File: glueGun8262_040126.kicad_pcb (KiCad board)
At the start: 2 copper layers, 104 x 93 mm, 73 parts, among them CN1 KF243-5.0-2P, CN2 KF243-5.0-2P, CN3 KF243-5.0-2P, CN4 KF243-5.0-2P, CN5 KF243-5.0-2P, CN6 KF243-5.0-2P, CN7 KF243-5.0-2P, CN9 KF243-5.0-4P, Q1 SQM120P10-10m1L, U1 DRV8262DDWR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

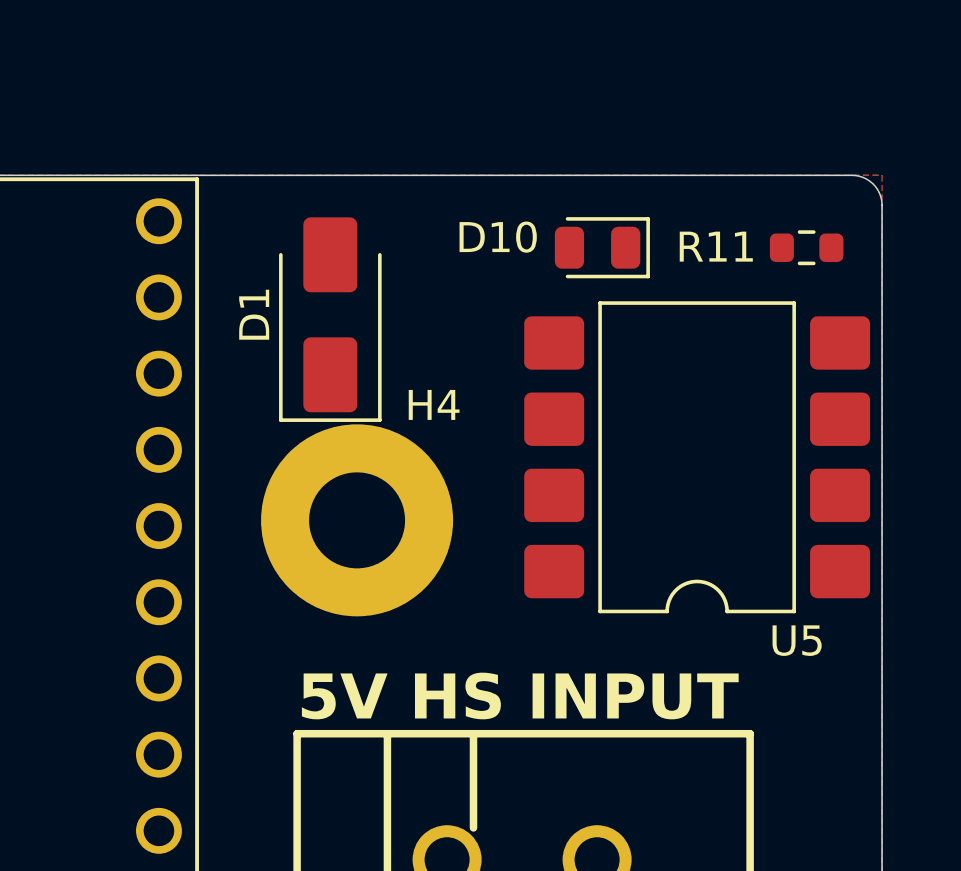
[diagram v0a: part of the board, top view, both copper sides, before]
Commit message: minor relocation
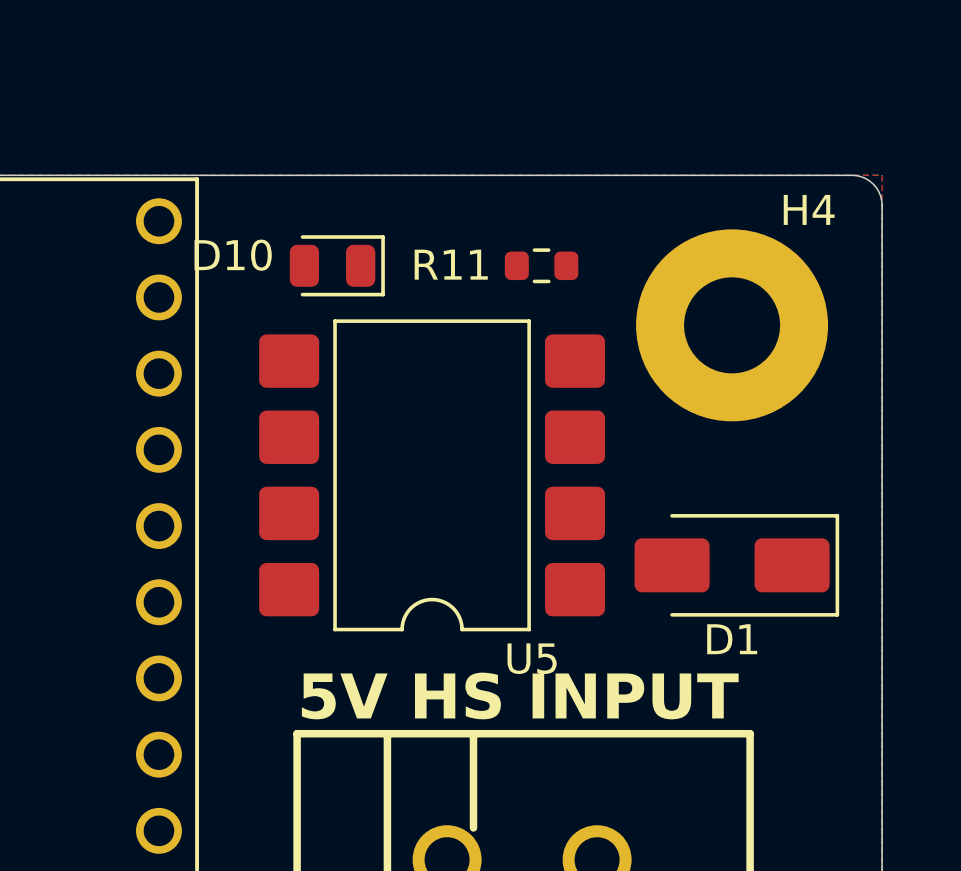
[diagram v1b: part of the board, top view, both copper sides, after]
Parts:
- moved D1 15.8 mm to (205.0, 53.0), turned to 180 degrees
- moved H4 14.1 mm to (205.0, 45.0)
- moved D10 8.86 mm to (191.7, 43.0)
- moved R11 8.86 mm to (198.7, 43.0)
- moved U5 8.86 mm to (195.0, 50.0)
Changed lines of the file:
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@@
 	(footprint "Resistor_SMD:R_0603_1608Metric"
 		(layer "F.Cu")
-		(at 207.4863 42.4125)
+		(at 198.6513 43.015)
 		(descr "Resistor SMD 0603 (1608 Metric), square (rectangular) end terminal, IPC-7351 nominal, (Body size source: IPC-SM-782 page 72, https://www.pcb-3d.com/wordpress/wp-content/uploads/ipc-sm-782a_amendment_1_and_2.pdf), generated with kicad-footprint-generator")
 		(tags "resistor")
@@
 	(footprint "LED_SMD:LED_0805_2012Metric"
 		(layer "F.Cu")
-		(at 200.5163 42.4125 180)
+		(at 191.6813 43.015 180)
 		(descr "LED SMD 0805 (2012 Metric), square (rectangular) end terminal, IPC-7351 nominal, (Body size source: https://docs.google.com/spreadsheets/d/1BsfQQcO9C6DZCsRaXUlFlo91Tg2WpOkGARC1WS5S8t0/edit?usp=sharing), generated with kicad-footprint-generator")
 		(tags "LED")
@@
 	(footprint "MountingHole:MountingHole_3.2mm_M3_Pad"
 		(layer "F.Cu")
-		(at 192.5 51.5)
+		(at 205 45)
 		(descr "Mounting Hole 3.2mm, M3, generated by kicad-footprint-generator mountinghole.py")
 		(tags "mountinghole M3")
@@
 	(footprint "Diode_SMD:D_SMA"
 		(layer "F.Cu")
-		(at 191.6088 44.65 90)
+		(at 205 53 180)
 		(descr "Diode SMA (DO-214AC)")
 		(tags "Diode SMA (DO-214AC)")
 		(property "Reference" "D1"
-			(at 0 -2.5 90)
+			(at 0 -2.5 0)
 			(layer "F.SilkS")
 			(effects
@@
 		)
 		(property "Value" "reverse protection"
-			(at 0 2.6 90)
+			(at 0 2.6 0)
 			(layer "F.Fab")
 			(effects
@@
 		)
 		(property "Datasheet" ""
-			(at 0 0 90)
+			(at 0 0 180)
 			(unlocked yes)
 			(layer "F.Fab")
@@
 		)
 		(property "Description" "Schottky diode"
-			(at 0 0 90)
+			(at 0 0 180)
 			(unlocked yes)
 			(layer "F.Fab")
@@
 		)
 		(property "part" "ss14"
-			(at 0 0 90)
+			(at 0 0 180)
 			(unlocked yes)
 			(layer "F.Fab")
@@
 		(attr smd)
 		(fp_line
-			(start -3.51 -1.65)
-			(end 2 -1.65)
+			(start -3.51 1.65)
+			(end 2 1.65)
 			(stroke
 				(width 0.12)
@@
 		(fp_line
 			(start -3.51 -1.65)
-			(end -3.51 1.65)
+			(end 2 -1.65)
 			(stroke
 				(width 0.12)
@@
 		)
 		(fp_line
-			(start -3.51 1.65)
-			(end 2 1.65)
+			(start -3.51 -1.65)
+			(end -3.51 1.65)
 			(stroke
 				(width 0.12)
@@
 		)
 		(fp_line
-			(start 3.5 -1.75)
-			(end 3.5 1.75)
+			(start 3.5 1.75)
+			(end -3.5 1.75)
 			(stroke
 				(width 0.05)
@@
 		)
 		(fp_line
-			(start -3.5 -1.75)
-			(end 3.5 -1.75)
+			(start 3.5 -1.75)
+			(end 3.5 1.75)
 			(stroke
 				(width 0.05)
@@
 		)
 		(fp_line
-			(start 3.5 1.75)
-			(end -3.5 1.75)
+			(start -3.5 1.75)
+			(end -3.5 -1.75)
 			(stroke
 				(width 0.05)
@@
 		)
 		(fp_line
-			(start -3.5 1.75)
-			(end -3.5 -1.75)
+			(start -3.5 -1.75)
+			(end 3.5 -1.75)
 			(stroke
 				(width 0.05)
@@
 		)
 		(fp_line
-			(start 2.3 -1.5)
-			(end -2.3 -1.5)
+			(start 2.3 1.5)
+			(end -2.3 1.5)
 			(stroke
 				(width 0.1)
@@
 		)
 		(fp_line
-			(start -0.64944 -0.79908)
-			(end -0.64944 0.80112)
+			(start 2.3 -1.5)
+			(end -2.3 -1.5)
 			(stroke
 				(width 0.1)
@@
 		)
 		(fp_line
-			(start 0.50118 0.00102)
-			(end 1.4994 0.00102)
+			(start 0.50118 0.75032)
+			(end 0.50118 -0.79908)
 			(stroke
 				(width 0.1)
@@
 		)
 		(fp_line
-			(start -0.64944 0.00102)
-			(end 0.50118 -0.79908)
+			(start 0.50118 0.00102)
+			(end 1.4994 0.00102)
 			(stroke
 				(width 0.1)
@@
 		(fp_line
 			(start -0.64944 0.00102)
-			(end -1.55114 0.00102)
+			(end 0.50118 0.75032)
 			(stroke
 				(width 0.1)
@@
 		(fp_line
 			(start -0.64944 0.00102)
-			(end 0.50118 0.75032)
+			(end 0.50118 -0.79908)
 			(stroke
 				(width 0.1)
@@
 		)
 		(fp_line
-			(start 0.50118 0.75032)
-			(end 0.50118 -0.79908)
+			(start -0.64944 0.00102)
+			(end -1.55114 0.00102)
 			(stroke
 				(width 0.1)
@@
 		)
 		(fp_line
-			(start 2.3 1.5)
-			(end -2.3 1.5)
+			(start -0.64944 -0.79908)
+			(end -0.64944 0.80112)
 			(stroke
 				(width 0.1)
@@
 		)
 		(fp_text user "${REFERENCE}"
-			(at 0 -2.5 90)
+			(at 0 -2.5 0)
 			(layer "F.Fab")
 			(effects
@@
 		)
 		(pad "1" smd roundrect
-			(at -2 0 90)
+			(at -2 0 180)
 			(size 2.5 1.8)
 			(layers "F.Cu" "F.Mask" "F.Paste")
@@
 		)
 		(pad "2" smd roundrect
-			(at 2 0 90)
+			(at 2 0 180)
 			(size 2.5 1.8)
 			(layers "F.Cu" "F.Mask" "F.Paste")
@@
 	(footprint "Package_DIP:SMDIP-8_W9.53mm"
 		(layer "F.Cu")
-		(at 203.835 49.3975 180)
+		(at 195 50 180)
 		(descr "8-lead surface-mounted (SMD) DIP package, row spacing 9.53mm (375 mils)")
 		(tags "SMD DIP DIL PDIP SMDIP 2.54mm 9.53mm 375mil")

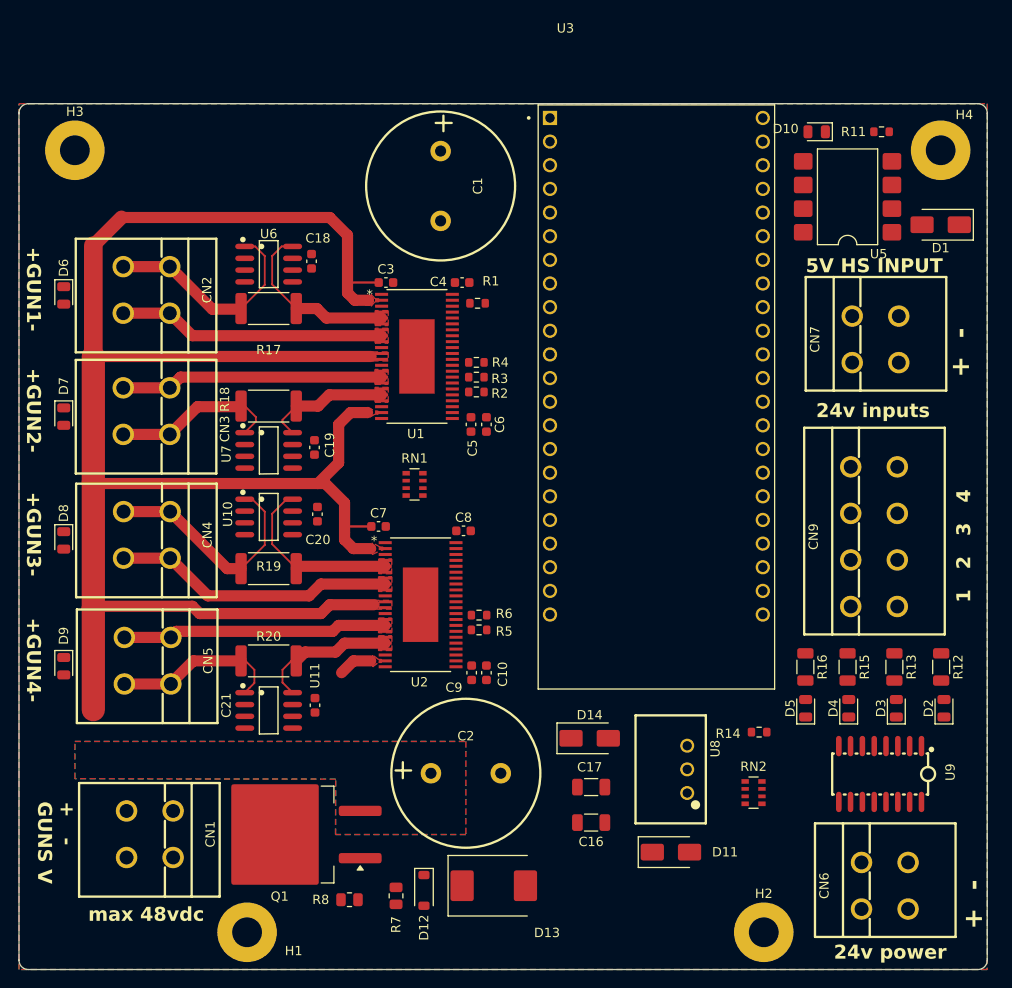
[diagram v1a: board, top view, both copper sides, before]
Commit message: redesign rectanglular board routed no errors
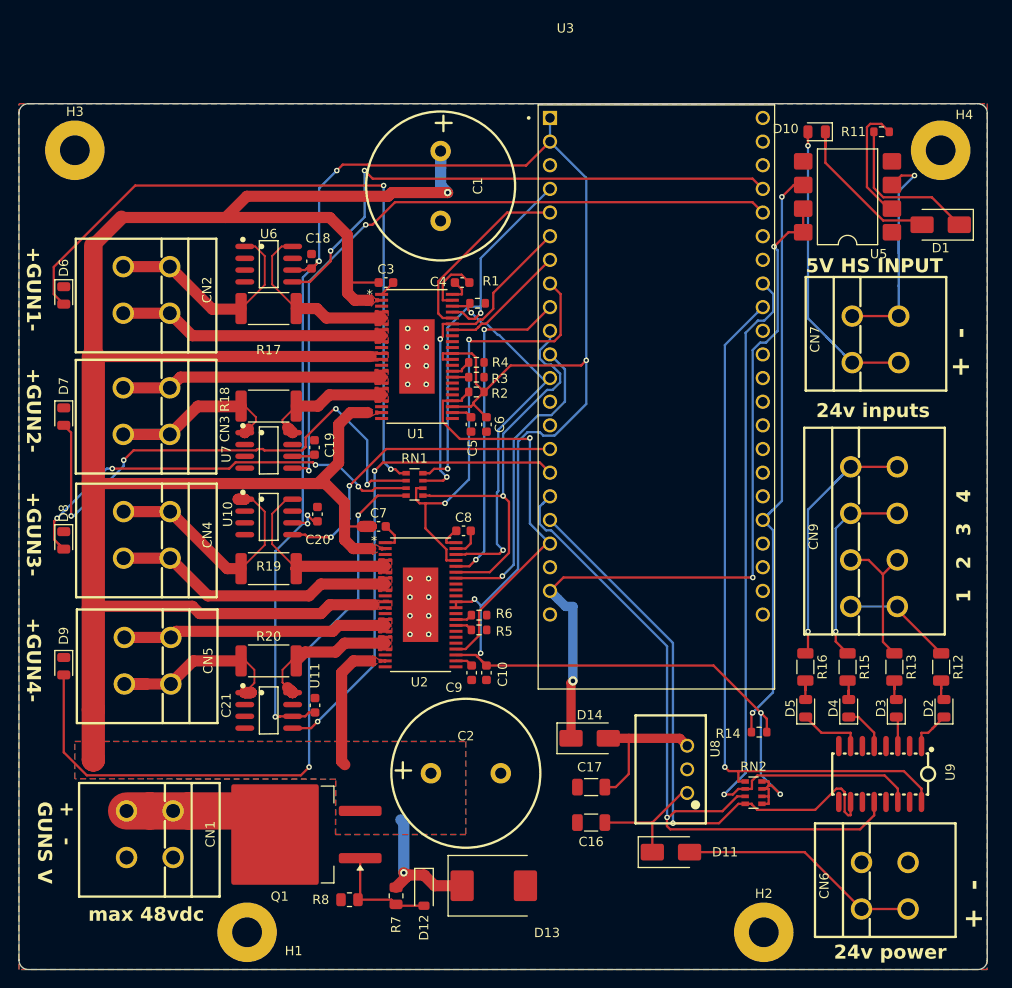
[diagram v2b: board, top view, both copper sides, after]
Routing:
- net +3V3: track 0.00 -> 253.7 mm, vias 0 -> 10
- net +5V: track 0.00 -> 85.1 mm, vias 0 -> 3
- net /Input_2_24v: track 0.00 -> 80.2 mm, vias 0 -> 1
- net /Input_1_24v: track 0.00 -> 77.3 mm, vias 0 -> 1
- net Net-(D6-A): track 0.00 -> 76.1 mm, vias 0 -> 2
- net /Input_3_24v: track 0.00 -> 76.0 mm, vias 0 -> 1
- net /Gun2Vref: track 0.00 -> 74.9 mm, vias 0 -> 2
- net Net-(D9-A): track 0.00 -> 71.3 mm, vias 0 -> 2
- net /Input_0_5v: track 0.00 -> 64.9 mm, vias 0 -> 2
- net +48V: track 204.0 -> 267.9 mm, vias 0 -> 2
- net /Input_4_24v: track 0.00 -> 63.1 mm, vias 0 -> 1
- net /Gun1Vref: track 0.00 -> 59.8 mm, vias 0 -> 2
- net Net-(D7-A): track 0.00 -> 58.3 mm, vias 0 -> 4
- net /Gun4Vref: track 0.00 -> 52.1 mm, vias 0 -> 2
- net /U2_IN1: track 0.00 -> 48.2 mm, vias 0 -> 2
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
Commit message: bulk cap rotated
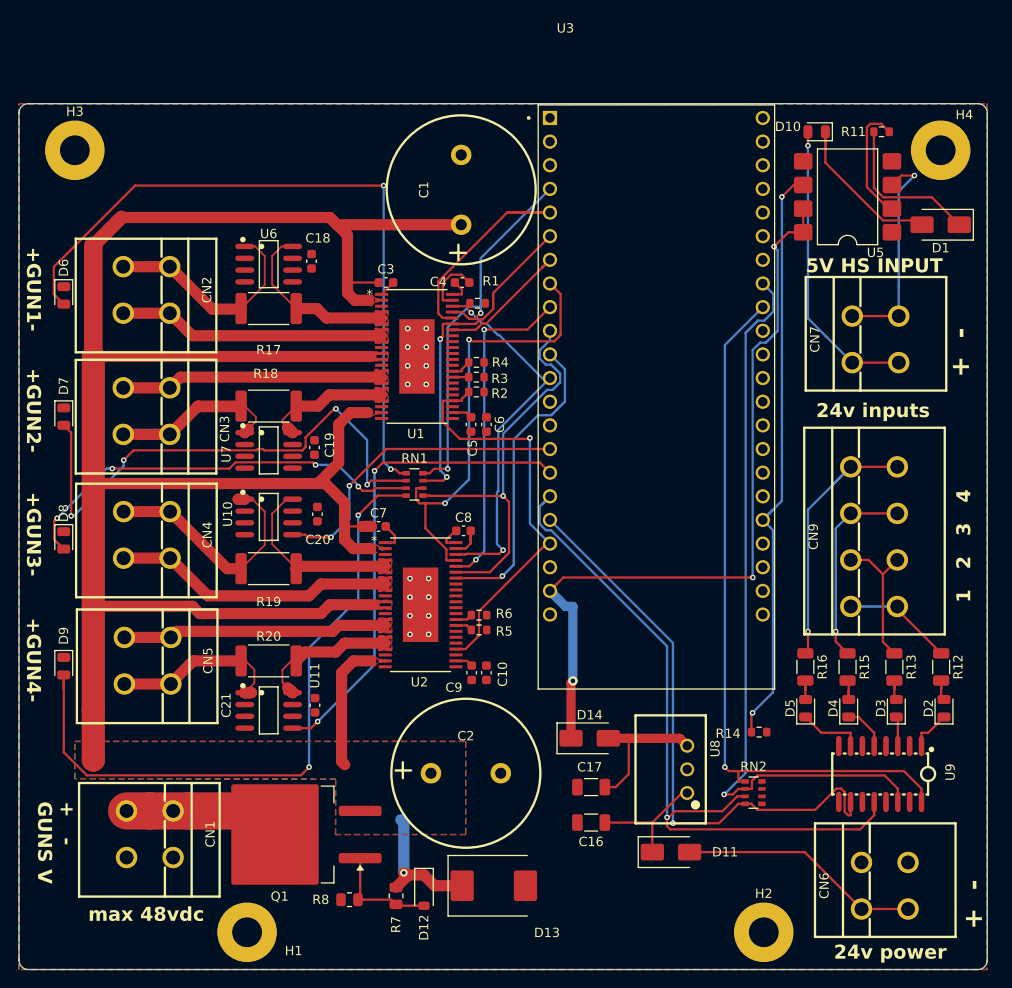
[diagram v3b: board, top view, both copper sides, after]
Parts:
- moved C1 2.25 mm to (153.5, 49.2), turned to 90 degrees
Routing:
- net +3V3: track 253.7 -> 0.00 mm, vias 10 -> 0
- net /Gun2Vref: track 74.9 -> 0.00 mm, vias 2 -> 0
- net /Gun1Vref: track 59.8 -> 0.00 mm, vias 2 -> 0
- net +48V: track 267.9 -> 251.6 mm, vias 2 -> 1
- net /U1_IN2: track 20.2 -> 24.6 mm
- net Net-(U11-IN-): track 24.1 -> 21.7 mm
- net Net-(U5-C): track 25.7 -> 23.6 mm
- net Net-(D10-A): track 34.5 -> 32.4 mm
- net Net-(D9-A): track 71.3 -> 72.8 mm
- net /U1_IN4: track 13.6 -> 14.8 mm
- net Net-(U2-CPL/DVDD): track 3.17 -> 4.23 mm
- net +5V: track 85.1 -> 86.1 mm
- net Net-(D2-K): track 5.45 -> 4.55 mm
- net /U1_OUT3: track 14.9 -> 15.7 mm
- net /Input_4_24v: track 63.1 -> 63.7 mm

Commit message: cap place correction
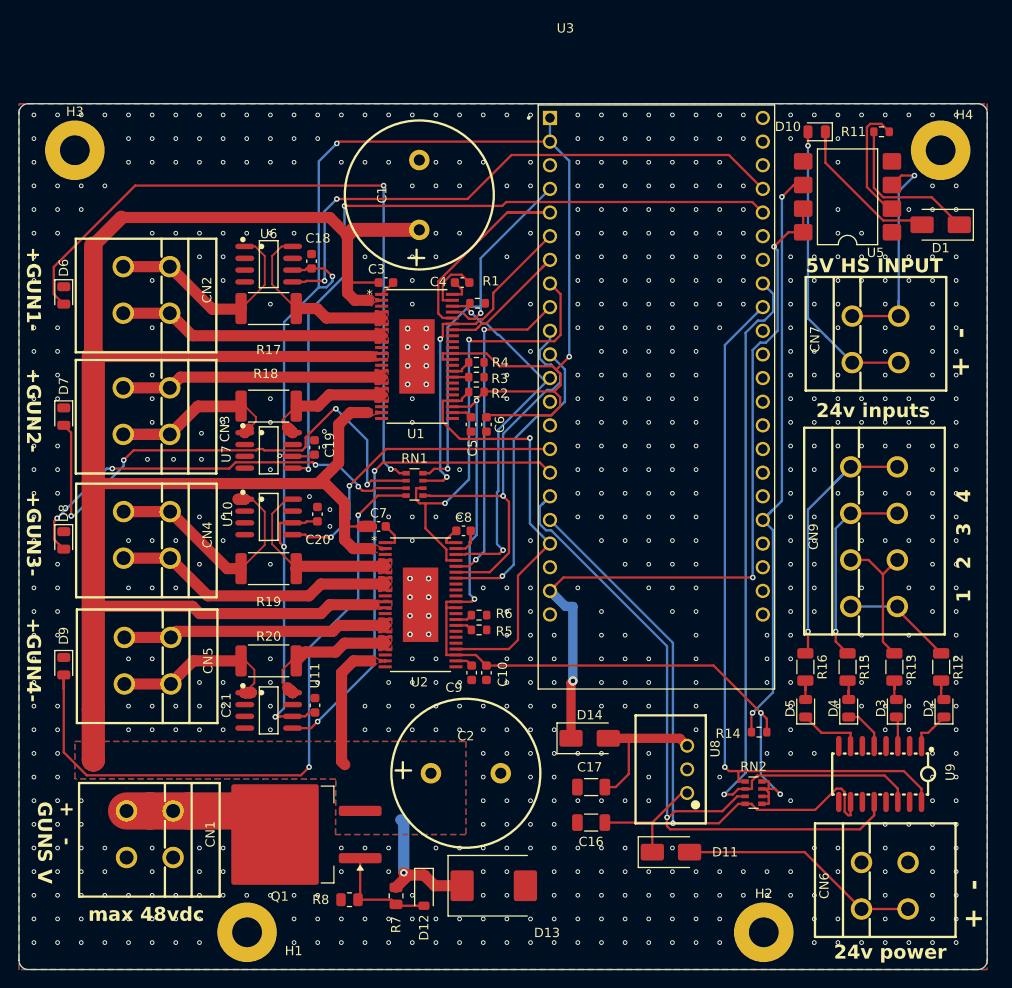
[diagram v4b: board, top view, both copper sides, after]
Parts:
- moved C1 4.53 mm to (149.0, 49.8)
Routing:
- net +3V3: track 0.00 -> 264.7 mm, vias 0 -> 10
- net /Gun2Vref: track 0.00 -> 77.2 mm, vias 0 -> 2
- net /Gun1Vref: track 0.00 -> 62.0 mm, vias 0 -> 2
- net +48V: track 251.6 -> 246.2 mm
- net /nFAULT: track 44.3 -> 46.8 mm
- net Net-(U5-C): track 23.6 -> 25.2 mm
- net Net-(D1-A): track 17.3 -> 18.1 mm
- net GND: vias 16 -> 727

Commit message: dont remember
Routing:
- net Net-(D9-A): track 72.8 -> 65.9 mm
- net +48V: track 246.2 -> 246.5 mm, vias 1 -> 40
